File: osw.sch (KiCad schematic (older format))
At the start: 62 parts, among them J1 Conn_01x02, Q1 2N7002, SW1 SW_Push, SW2 SW_Push, SW4 SW_Push, SW5 SW_Push, U1 DS3231MZ, U10 XC6209, U11 MCP73831T-2ACI_OT, U12 USBLC6-2SC6, U13 XC6209, U2 BMA400, U3 BMP280, U4 GC9A01_IPS_display, U5 USB-OTG, U6 CH340E, U7 ttgo-32-micro, U8 Quectel_L96, U9 TPS2115A

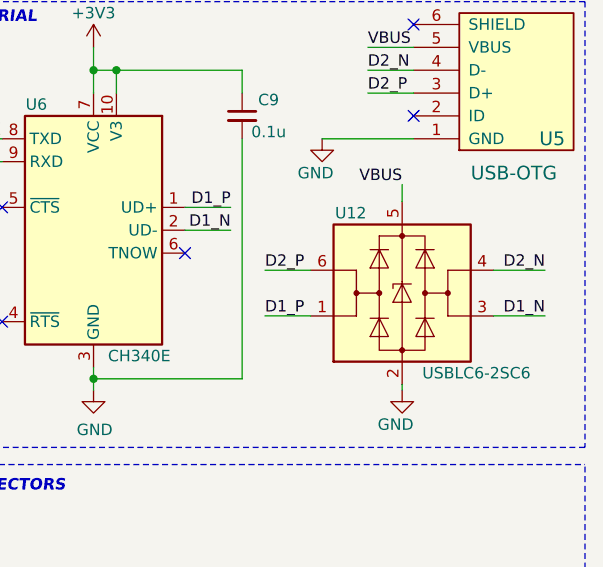
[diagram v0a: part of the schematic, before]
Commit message: update PCB, place components randomly
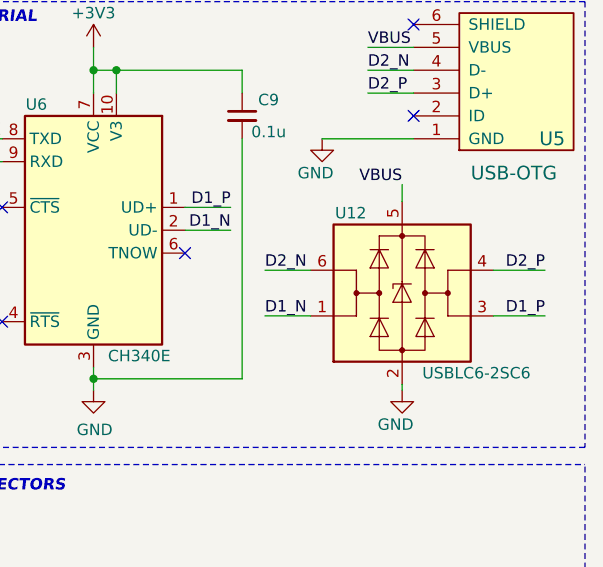
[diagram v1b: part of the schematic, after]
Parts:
- R5: footprint Resistor_SMD:R_0603_1608Metric -> Resistor_SMD:R_0402_1005Metric
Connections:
- net D1_N: now also U12.1 (I/O1); no longer U12.3 (I/O2)
- net D1_P: now also U12.3 (I/O2); no longer U12.1 (I/O1)
- net D2_N: now also U12.6 (I/O1); no longer U12.4 (I/O2)
- net D2_P: now also U12.4 (I/O2); no longer U12.6 (I/O1)
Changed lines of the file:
@@
 F 0 "R5" V 650 3200 50  0000 C CNN
 F 1 "0R" V 825 3200 50  0000 C CNN
-F 2 "Resistor_SMD:R_0603_1608Metric" H 750 3200 50  0001 C CNN
+F 2 "Resistor_SMD:R_0402_1005Metric" H 750 3200 50  0001 C CNN
 F 3 "~" H 750 3200 50  0001 C CNN
 	1    750  3200
@@
 Wire Wire Line
 	10300 4200 10300 4175
+Text Label 10925 3875 2    50   ~ 0
+D1_P
+Wire Wire Line
+	9700 3875 9900 3875
+Wire Wire Line
+	9700 3675 9900 3675
+Wire Wire Line
+	8375 3150 8375 3200
+Wire Wire Line
+	8375 3200 8550 3200
+Wire Wire Line
+	10925 3675 10700 3675
 Text Label 9700 3875 0    50   ~ 0
-D1_P
-Wire Wire Line
-	9700 3875 9900 3875
-Text Label 9700 3675 0    50   ~ 0
-D2_P
-Wire Wire Line
-	9700 3675 9900 3675
-Wire Wire Line
-	8375 3150 8375 3200
-Wire Wire Line
-	8375 3200 8550 3200
-Text Label 10925 3675 2    50   ~ 0
-D2_N
-Wire Wire Line
-	10925 3675 10700 3675
-Text Label 10925 3875 2    50   ~ 0
 D1_N
 Wire Wire Line
@@
 	1    0    0    -1
 $EndComp
+Text Label 9700 3675 0    50   ~ 0
+D2_N
+Text Label 10925 3675 2    50   ~ 0
+D2_P
 $EndSCHEMATC

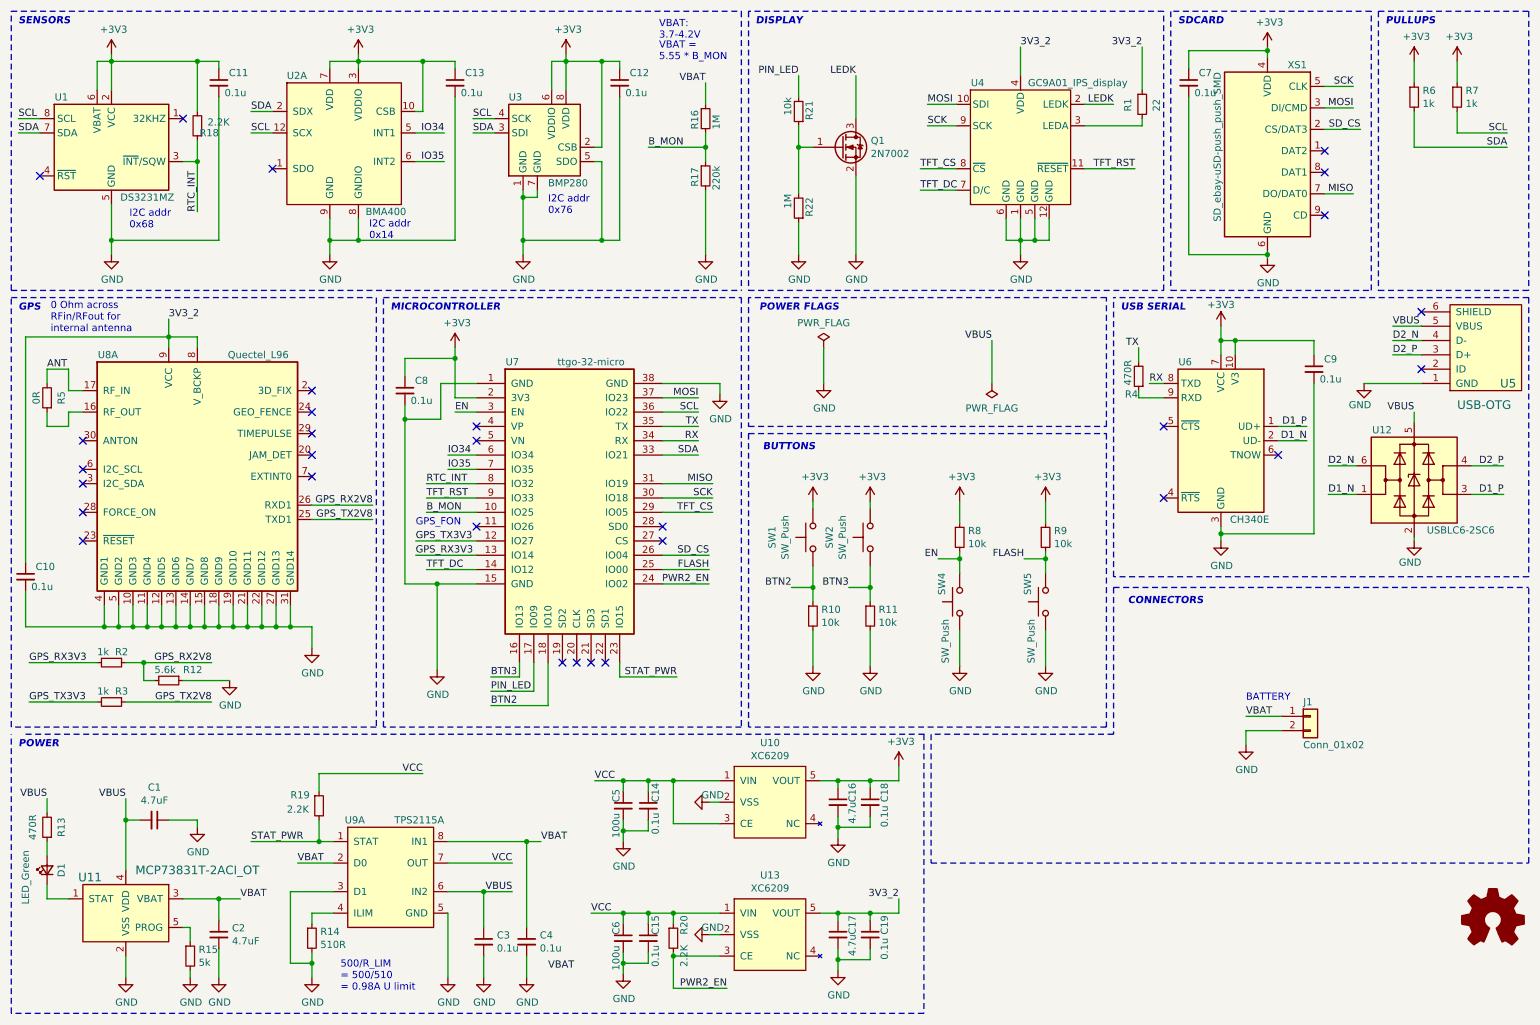
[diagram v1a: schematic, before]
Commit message: update board to rev2.0
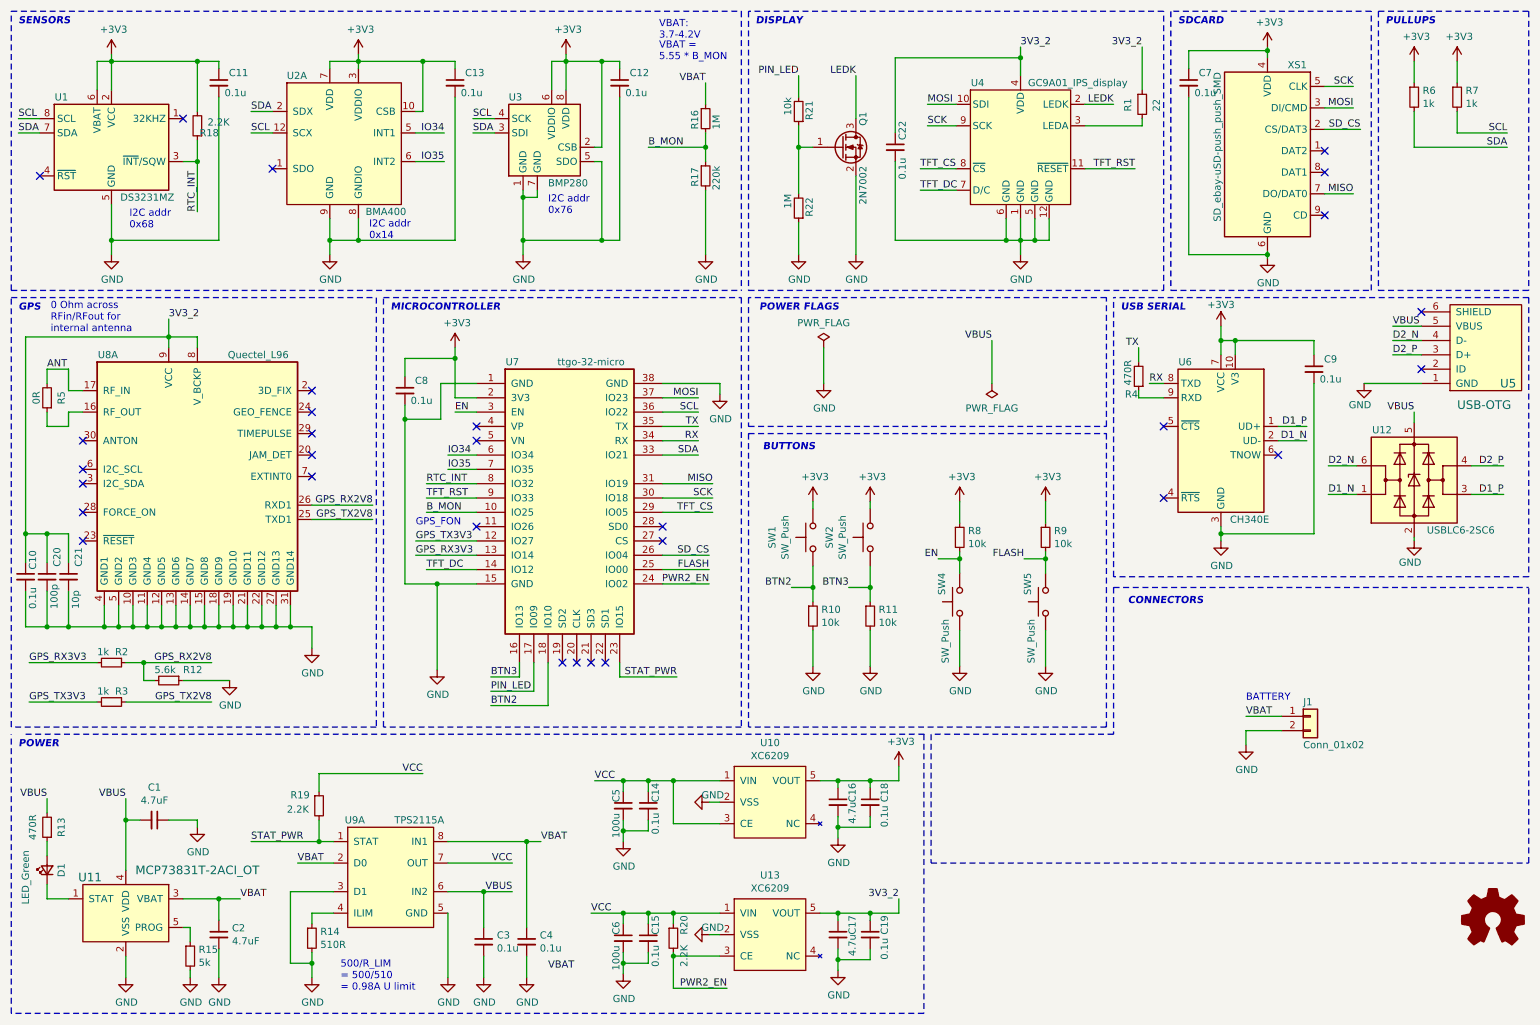
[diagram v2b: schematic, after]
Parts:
- added C20: 100p, Capacitor_SMD:C_0603_1608Metric, symbol Device:C_Small
- added C21: 10p, Capacitor_SMD:C_0603_1608Metric, symbol Device:C_Small
- added C22: 0.1u, Capacitor_SMD:C_0603_1608Metric, symbol Device:C_Small
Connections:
- net 3V3_2: now also C20.1, C21.1, C22.1
- net GND: now also C20.2, C21.2, C22.2
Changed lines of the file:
@@
 	7100 1300 6900 1300
 Wire Wire Line
-	7550 750  7550 950
+	7550 750  7550 825
 Wire Wire Line
 	7450 1950 7450 2100
@@
 U 1 1 5F61875A
 P 6300 1450
-F 0 "Q1" H 6504 1496 50  0000 L CNN
-F 1 "2N7002" H 6504 1405 50  0000 L CNN
+F 0 "Q1" V 6450 1600 50  0000 L CNN
+F 1 "2N7002" V 6450 1050 50  0000 L CNN
 F 2 "Package_TO_SOT_SMD:SOT-23" H 6500 1375 50  0001 L CIN
 F 3 "https://www.fairchildsemi.com/datasheets/2N/2N7002.pdf" H 6300 1450 50  0001 L CNN
@@
 U 1 1 5F827434
 P 600 4450
-F 0 "C10" H 670 4520 50  0000 L CNN
-F 1 "0.1u" H 640 4380 50  0000 L CNN
+F 0 "C10" V 650 4500 50  0000 L CNN
+F 1 "0.1u" V 650 4225 50  0000 L CNN
 F 2 "Capacitor_SMD:C_0603_1608Metric" H 600 4450 50  0001 C CNN
 F 3 "~" H 600 4450 50  0001 C CNN
@@
 	9950 3100 10350 3100
 Wire Wire Line
-	1150 4800 600  4800
+	1150 4800 900  4800
 Wire Wire Line
 	600  4800 600  4550
@@
 	1600 2775 600  2775
 Wire Wire Line
-	600  2775 600  4350
+	600  2775 600  4150
 Connection ~ 2450 4800
 Wire Wire Line
@@
 Text Label 10925 3675 2    50   ~ 0
 D2_P
+$Comp
+L Device:C_Small C22
+U 1 1 5FB6680D
+P 6675 1450
+F 0 "C22" V 6725 1500 50  0000 L CNN
+F 1 "0.1u" V 6725 1225 50  0000 L CNN
+F 2 "Capacitor_SMD:C_0603_1608Metric" H 6675 1450 50  0001 C CNN
+F 3 "~" H 6675 1450 50  0001 C CNN
+	1    6675 1450
+	1    0    0    -1
+$EndComp
+Wire Wire Line
+	7550 825  6675 825
+Wire Wire Line
+	6675 825  6675 1350
+Connection ~ 7550 825
+Wire Wire Line
+	7550 825  7550 950
+Wire Wire Line
+	6675 1550 6675 2100
+Wire Wire Line
+	6675 2100 7450 2100
+Connection ~ 7450 2100
+$Comp
+L Device:C_Small C21
+U 1 1 5FBADDF0
+P 900 4450
+F 0 "C21" V 970 4520 50  0000 L CNN
+F 1 "10p" V 950 4225 50  0000 L CNN
+F 2 "Capacitor_SMD:C_0603_1608Metric" H 900 4450 50  0001 C CNN
+F 3 "~" H 900 4450 50  0001 C CNN
+	1    900  4450
+	1    0    0    -1
+$EndComp
+$Comp
+L Device:C_Small C20
+U 1 1 5FBAD886
+P 750 4450
+F 0 "C20" V 820 4520 50  0000 L CNN
+F 1 "100p" V 800 4225 50  0000 L CNN
+F 2 "Capacitor_SMD:C_0603_1608Metric" H 750 4450 50  0001 C CNN
+F 3 "~" H 750 4450 50  0001 C CNN
+	1    750  4450
+	1    0    0    -1
+$EndComp
+Wire Wire Line
+	750  4350 750  4150
+Wire Wire Line
+	750  4150 600  4150
+Connection ~ 600  4150
+Wire Wire Line
+	600  4150 600  4350
+Wire Wire Line
+	750  4150 900  4150
+Wire Wire Line
+	900  4150 900  4350
+Connection ~ 750  4150
+Wire Wire Line
+	750  4550 750  4800
+Connection ~ 750  4800
+Wire Wire Line
+	750  4800 600  4800
+Wire Wire Line
+	900  4550 900  4800
+Connection ~ 900  4800
+Wire Wire Line
+	900  4800 750  4800
 $EndSCHEMATC
